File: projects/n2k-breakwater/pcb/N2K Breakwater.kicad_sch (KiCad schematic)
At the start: 44 parts, among them J1 Shield to Ground, J2 N2K, J3 Signals, J4 Power, Q1 SQJ872EP-T1_BE3, Q2 SQJ872EP-T1_BE3, Q3 BSS123NH6327XTSA1, Q4 BSS126H6327XTSA2

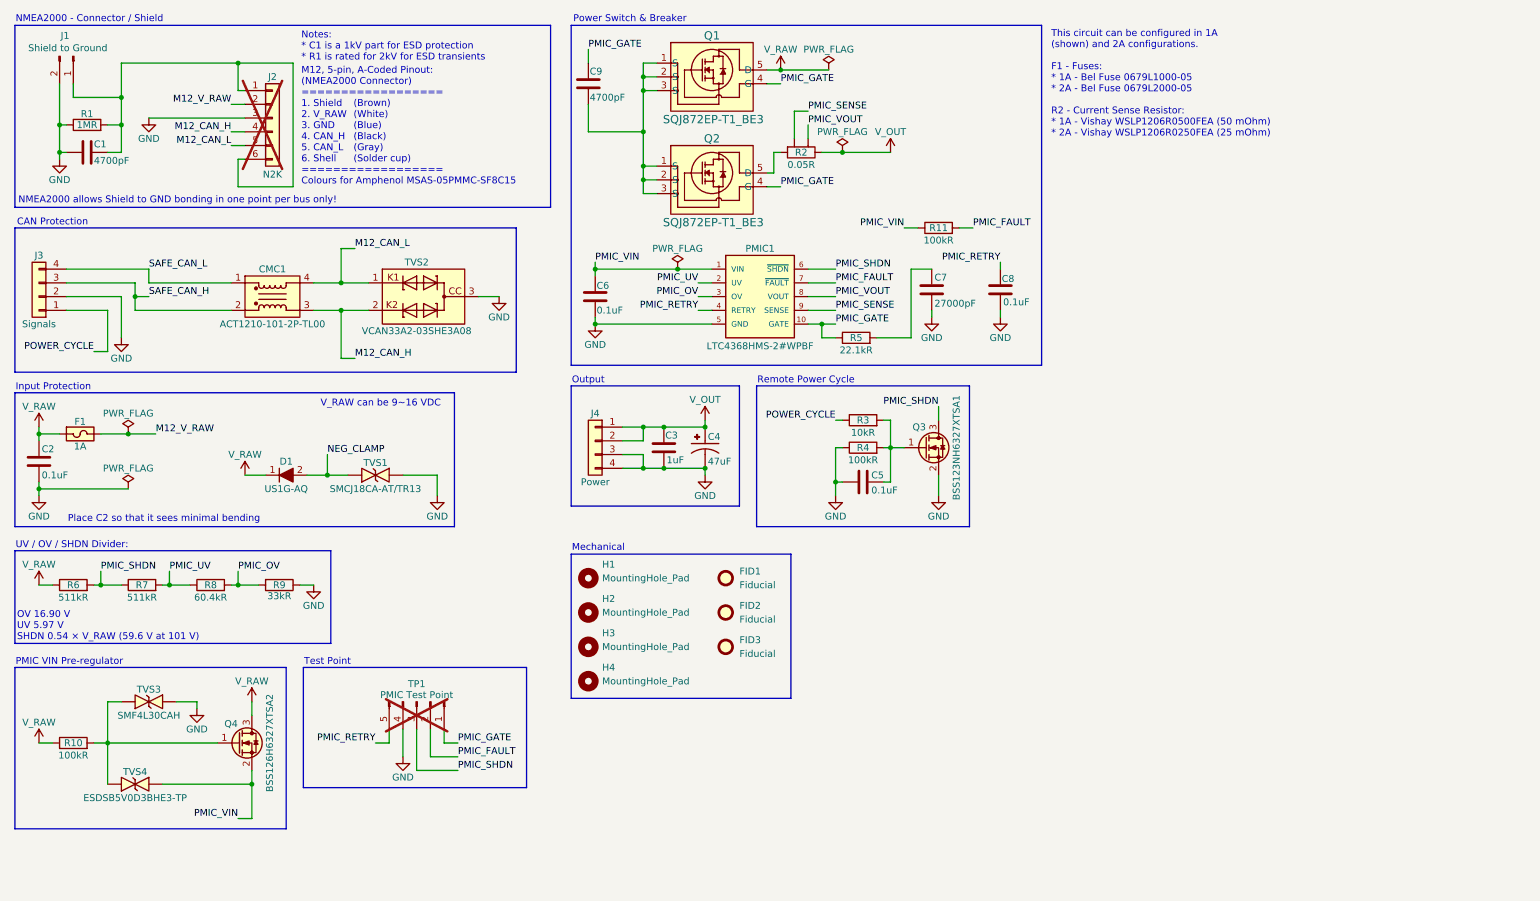
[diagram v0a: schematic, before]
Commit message: Added zip-tie slots to allow strain relief.
Signed-off-by: digimer <digital.mermaid@gmail.com>
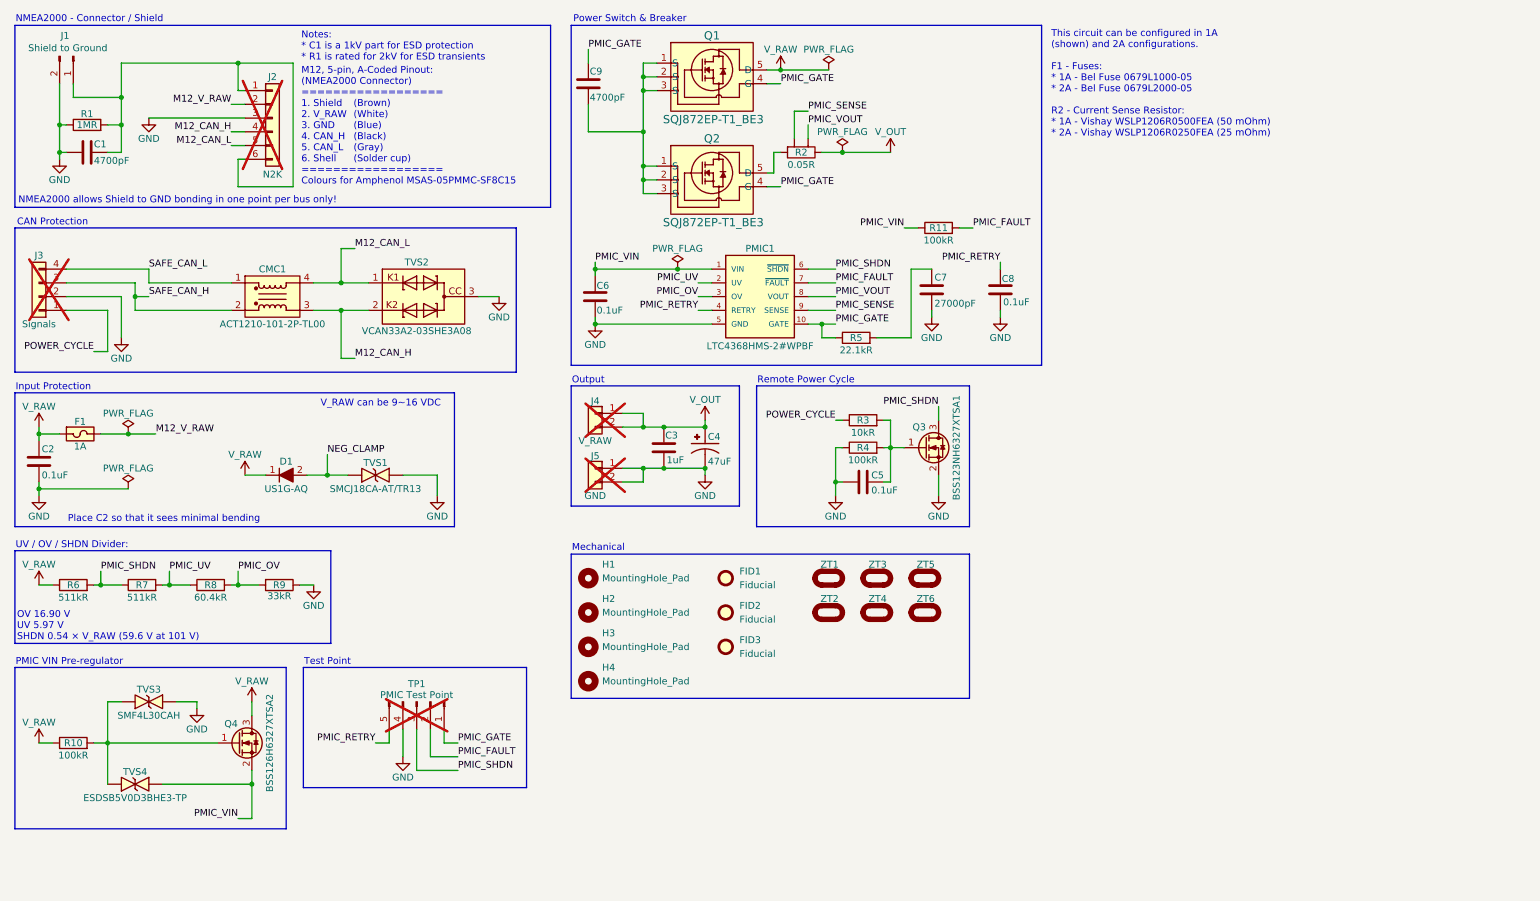
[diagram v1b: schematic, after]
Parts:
- removed J4: Power, Connector_PinHeader_2.54mm:PinHeader_1x04_P2.54mm_Vertical, symbol Connector_Generic:Conn_01x04
- added J4: V_RAW, Connector_PinHeader_2.54mm:PinHeader_1x02_P2.54mm_Vertical, symbol Connector_Generic:Conn_01x02
- added J5: GND, Connector_PinHeader_2.54mm:PinHeader_1x02_P2.54mm_Vertical, symbol Connector_Generic:Conn_01x02
- added ZT1, ZT2, ZT3, ZT4, ZT5, ZT6: (no value), mr-stuff:Tuskar Ziptie Slot 4.5x2mm, symbol mr-parts:Tuskar Ziptie slot 4.5x2mm
- J3: now not fitted; now left out of the parts list
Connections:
- net GND: now also J5.1 (Pin_1), J5.2 (Pin_2)
- net V_OUT: now also J4.1 (Pin_1), J4.2 (Pin_2)

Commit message: Fixed DRC issues.
Signed-off-by: digimer <digital.mermaid@gmail.com>
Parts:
- renumbered C9 to C3, C6 to C4, C7 to C5, C8 to C6, C3 to C7, C4 to C8, C5 to C9, Q4 to Q1, Q1 to Q2, Q2 to Q3, Q3 to Q4, R3 to R10, R4 to R11, R6 to R2, R7 to R3, R8 to R4, R9 to R5, R10 to R6, R2 to R7, R11 to R8, R5 to R9, TVS2 to TVS1, TVS1 to TVS2
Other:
- note added: "This circuit can be configured in 1A (shown) and 2A configurations. F1 - Fuses: * 1A - Bel Fuse 0679L1000-05 * 2A - Bel Fuse 0679L2000-05 R7 - Current Sense Resistor: * 1A - Vishay WSLP1206R0500FEA (50 mOhm) * 2A - Vishay WSLP1206R0250FEA (25 mOhm)"
- note removed: "This circuit can be configured in 1A (shown) and 2A configurations. F1 - Fuses: * 1A - Bel Fuse 0679L1000-05 * 2A - Bel Fuse 0679L2000-05 R2 - Current Sense Resistor: * 1A - Vishay WSLP1206R0500FEA (50 mOhm) * 2A - Vishay WSLP1206R0250FEA (25 mOhm)"
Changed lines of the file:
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@@
 		)
 	)
-	(text "This circuit can be configured in 1A \n(shown) and 2A configurations.\n\nF1 - Fuses:\n* 1A - Bel Fuse 0679L1000-05\n* 2A - Bel Fuse 0679L2000-05\n\nR2 - Current Sense Resistor:\n* 1A - Vishay WSLP1206R0500FEA (50 mOhm)\n* 2A - Vishay WSLP1206R0250FEA (25 mOhm)"
+	(text "This circuit can be configured in 1A \n(shown) and 2A configurations.\n\nF1 - Fuses:\n* 1A - Bel Fuse 0679L1000-05\n* 2A - Bel Fuse 0679L2000-05\n\nR7 - Current Sense Resistor:\n* 1A - Vishay WSLP1206R0500FEA (50 mOhm)\n* 2A - Vishay WSLP1206R0250FEA (25 mOhm)"
 		(exclude_from_sim no)
 		(at 206.248 16.764 0)
@@
 		(in_pos_files yes)
 		(dnp no)
-		(property "Reference" "R4"
+		(property "Reference" "R11"
 			(at 171.45 93.98 0)
 			(show_name no)
@@
 			(project "N2K Breakwater"
 				(path "/2a070473-cb6e-4844-8f2a-5ea6a35ddb49"
-					(reference "R4")
+					(reference "R11")
 					(unit 1)
 				)
@@
 		(in_pos_files yes)
 		(dnp no)
-		(property "Reference" "Q3"
+		(property "Reference" "Q4"
 			(at 180.594 90.17 0)
 			(show_name no)
@@
 			(project "N2K Breakwater"
 				(path "/2a070473-cb6e-4844-8f2a-5ea6a35ddb49"
-					(reference "Q3")
+					(reference "Q4")
 					(unit 1)
 				)
@@
 		(in_pos_files yes)
 		(dnp no)
-		(property "Reference" "Q2"
+		(property "Reference" "Q3"
 			(at 143.51 36.83 0)
 			(show_name no)
@@
 			(project "N2K Breakwater"
 				(path "/2a070473-cb6e-4844-8f2a-5ea6a35ddb49"
-					(reference "Q2")
+					(reference "Q3")
 					(unit 1)
 				)
@@
 		(in_pos_files yes)
 		(dnp no)
-		(property "Reference" "C5"
+		(property "Reference" "C9"
 			(at 172.974 99.06 90)
 			(show_name no)
@@
 			(project "N2K Breakwater"
 				(path "/2a070473-cb6e-4844-8f2a-5ea6a35ddb49"
-					(reference "C5")
+					(reference "C9")
 					(unit 1)
 				)
@@
 		(in_pos_files yes)
 		(dnp no)
-		(property "Reference" "R9"
+		(property "Reference" "R5"
 			(at 63.5 119.38 0)
 			(show_name no)
@@
 			(project "N2K Breakwater"
 				(path "/2a070473-cb6e-4844-8f2a-5ea6a35ddb49"
-					(reference "R9")
+					(reference "R5")
 					(unit 1)
 				)
@@
 		(in_pos_files yes)
 		(dnp no)
-		(property "Reference" "C7"
+		(property "Reference" "C5"
 			(at 184.658 62.484 0)
 			(show_name no)
@@
 			(project "N2K Breakwater"
 				(path "/2a070473-cb6e-4844-8f2a-5ea6a35ddb49"
-					(reference "C7")
+					(reference "C5")
 					(unit 1)
 				)
@@
 		(in_pos_files yes)
 		(dnp no)
-		(property "Reference" "Q1"
+		(property "Reference" "Q2"
 			(at 143.51 17.78 0)
 			(show_name no)
@@
 			(project "N2K Breakwater"
 				(path "/2a070473-cb6e-4844-8f2a-5ea6a35ddb49"
-					(reference "Q1")
+					(reference "Q2")
 					(unit 1)
 				)
@@
 		(in_pos_files yes)
 		(dnp no)
-		(property "Reference" "Q4"
+		(property "Reference" "Q1"
 			(at 53.34 145.034 0)
 			(show_name no)
@@
 			(project "N2K Breakwater"
 				(path "/2a070473-cb6e-4844-8f2a-5ea6a35ddb49"
-					(reference "Q4")
+					(reference "Q1")
 					(unit 1)
 				)
@@
 		(in_pos_files yes)
 		(dnp no)
-		(property "Reference" "C3"
+		(property "Reference" "C7"
 			(at 134.874 91.694 0)
 			(show_name no)
@@
 			(project "N2K Breakwater"
 				(path "/2a070473-cb6e-4844-8f2a-5ea6a35ddb49"
-					(reference "C3")
+					(reference "C7")
 					(unit 1)
 				)
@@
 		(in_pos_files yes)
 		(dnp no)
-		(property "Reference" "R8"
+		(property "Reference" "R4"
 			(at 50.8 119.38 0)
 			(show_name no)
@@
 			(project "N2K Breakwater"
 				(path "/2a070473-cb6e-4844-8f2a-5ea6a35ddb49"
-					(reference "R8")
+					(reference "R4")
 					(unit 1)
 				)
@@
 		(in_pos_files yes)
 		(dnp no)
-		(property "Reference" "R6"
+		(property "Reference" "R2"
 			(at 25.4 119.38 0)
 			(show_name no)
@@
 			(project "N2K Breakwater"
 				(path "/2a070473-cb6e-4844-8f2a-5ea6a35ddb49"
-					(reference "R6")
+					(reference "R2")
 					(unit 1)
 				)
@@
 		(in_pos_files yes)
 		(dnp no)
-		(property "Reference" "C6"
+		(property "Reference" "C4"
 			(at 122.174 64.008 0)
 			(show_name no)
@@
 			(project "N2K Breakwater"
 				(path "/2a070473-cb6e-4844-8f2a-5ea6a35ddb49"
-					(reference "C6")
+					(reference "C4")
 					(unit 1)
 				)
@@
 		(in_pos_files yes)
 		(dnp no)
-		(property "Reference" "C8"
+		(property "Reference" "C6"
 			(at 197.104 62.738 0)
 			(show_name no)
@@
 			(project "N2K Breakwater"
 				(path "/2a070473-cb6e-4844-8f2a-5ea6a35ddb49"
-					(reference "C8")
+					(reference "C6")
 					(unit 1)
 				)
@@
 		(in_pos_files yes)
 		(dnp no)
-		(property "Reference" "R2"
+		(property "Reference" "R7"
 			(at 160.02 39.37 0)
 			(show_name no)
@@
 			(project "N2K Breakwater"
 				(path "/2a070473-cb6e-4844-8f2a-5ea6a35ddb49"
-					(reference "R2")
+					(reference "R7")
 					(unit 1)
 				)
@@
 		(in_pos_files yes)
 		(dnp no)
-		(property "Reference" "R5"
+		(property "Reference" "R9"
 			(at 170.18 73.66 0)
 			(show_name no)
@@
 			(project "N2K Breakwater"
 				(path "/2a070473-cb6e-4844-8f2a-5ea6a35ddb49"
-					(reference "R5")
+					(reference "R9")
 					(unit 1)
 				)
@@
 		(in_pos_files yes)
 		(dnp no)
-		(property "Reference" "R11"
+		(property "Reference" "R8"
 			(at 185.42 53.34 0)
 			(show_name no)
@@
 			(project "N2K Breakwater"
 				(path "/2a070473-cb6e-4844-8f2a-5ea6a35ddb49"
-					(reference "R11")
+					(reference "R8")
 					(unit 1)
 				)
@@
 		(in_pos_files yes)
 		(dnp no)
-		(property "Reference" "TVS1"
+		(property "Reference" "TVS2"
 			(at 81.28 96.774 0)
 			(show_name no)
@@
 			(project "N2K Breakwater"
 				(path "/2a070473-cb6e-4844-8f2a-5ea6a35ddb49"
-					(reference "TVS1")
+					(reference "TVS2")
 					(unit 1)
 				)
@@
 		(in_pos_files yes)
 		(dnp no)
-		(property "Reference" "C9"
+		(property "Reference" "C3"
 			(at 120.904 24.384 0)
 			(show_name no)
@@
 			(project "N2K Breakwater"
 				(path "/2a070473-cb6e-4844-8f2a-5ea6a35ddb49"
-					(reference "C9")
+					(reference "C3")
 					(unit 1)
 				)
@@
 		(in_pos_files yes)
 		(dnp no)
-		(property "Reference" "TVS2"
+		(property "Reference" "TVS1"
 			(at 88.9 59.69 0)
 			(show_name no)
@@
 			(project "N2K Breakwater"
 				(path "/2a070473-cb6e-4844-8f2a-5ea6a35ddb49"
-					(reference "TVS2")
+					(reference "TVS1")
 					(unit 1)
 				)
@@
 		(in_pos_files yes)
 		(dnp no)
-		(property "Reference" "R7"
+		(property "Reference" "R3"
 			(at 38.1 119.38 0)
 			(show_name no)
@@
 			(project "N2K Breakwater"
 				(path "/2a070473-cb6e-4844-8f2a-5ea6a35ddb49"
-					(reference "R7")
+					(reference "R3")
 					(unit 1)
 				)
@@
 		(in_pos_files yes)
 		(dnp no)
-		(property "Reference" "R10"
+		(property "Reference" "R6"
 			(at 25.4 148.59 0)
 			(show_name no)
@@
 			(project "N2K Breakwater"
 				(path "/2a070473-cb6e-4844-8f2a-5ea6a35ddb49"
-					(reference "R10")
+					(reference "R6")
 					(unit 1)
 				)
@@
 		(in_pos_files yes)
 		(dnp no)
-		(property "Reference" "R3"
+		(property "Reference" "R10"
 			(at 171.45 88.9 0)
 			(show_name no)
@@
 			(project "N2K Breakwater"
 				(path "/2a070473-cb6e-4844-8f2a-5ea6a35ddb49"
-					(reference "R3")
+					(reference "R10")
 					(unit 1)
 				)
@@
 		(in_pos_files yes)
 		(dnp no)
-		(property "Reference" "C4"
+		(property "Reference" "C8"
 			(at 142.748 91.948 90)
 			(show_name no)
@@
 			(project "N2K Breakwater"
 				(path "/2a070473-cb6e-4844-8f2a-5ea6a35ddb49"
-					(reference "C4")
+					(reference "C8")
 					(unit 1)
 				)

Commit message: Fixed J4's label to 'V_OUT'.
Signed-off-by: digimer <digital.mermaid@gmail.com>
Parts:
- J4: value V_RAW -> V_OUT
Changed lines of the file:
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@@
 			)
 		)
-		(property "Value" "V_RAW"
+		(property "Value" "V_OUT"
 			(at 121.92 92.71 0)
 			(show_name no)

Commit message: Reworked the PCB and F1+R7 values.
Signed-off-by: digimer <digital.mermaid@gmail.com>
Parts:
- removed J2: N2K, Connector_PinHeader_2.54mm:PinHeader_1x06_P2.54mm_Vertical, symbol Connector_Generic:Conn_01x06
- removed ZT5, ZT6: (no value), mr-stuff:Tuskar Ziptie Slot 4.5x2mm, symbol mr-parts:Tuskar Ziptie slot 4.5x2mm
- added J2: Shell, Connector_PinHeader_2.54mm:PinHeader_1x01_P2.54mm_Vertical, symbol Connector_Generic:Conn_01x01
- added TB1: 1862440, mr-stuff:Phoenix Contact 1862440, symbol mr-parts:Phoenix Contact 1862440
- F1: value 1A -> 2.5A; symbol mr-parts:Bel Fuse 0679L1000-05 -> mr-parts:Bel Fuse 0679L2500-05; Part Bel Fuse 0679L1000-05 -> Bel Fuse 0679L2500-05
- R7: value 0.05R -> 0.033R; footprint mr-stuff:Vishay WSLP 1206 4-wire Kelvin -> mr-stuff:Vishay RCWE 1206 4-wire Kelvin; symbol mr-parts:Vishay WSLP1206R0500FEA -> mr-parts:Vishay RCWE120633L0FNEA; Part Vishay WSLP1206R0500FEA -> Vishay RCWE120633L0FNEA
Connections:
- net GND: now also J3.3 (Pin_3), TB1.5, TB1.6; no longer J3.2 (Pin_2)
- net M12_CAN_H: now also TB1.7, TB1.8
- net M12_CAN_L: now also TB1.10, TB1.9
- net M12_V_RAW: now also TB1.3, TB1.4
- net POWER_CYCLE: now also J3.4 (Pin_4); no longer J3.1 (Pin_1)
- net SAFE_CAN_H: now also J3.1 (Pin_1); no longer J3.3 (Pin_3)
- net SAFE_CAN_L: now also J3.2 (Pin_2); no longer J3.4 (Pin_4)
- net at C1.2, J1.1 (Pin_1), R1.2: now also J2.1 (Pin_1), TB1.1, TB1.2
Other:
- note added: "- Brown - White - Blue - Black - Gray"
- note added: "M12, 5-pin, A-Coded Pinout: (NMEA2000 Connector) ================== 1. Shield 2. V_RAW 3. GND 4. CAN_H 5. CAN_L ================== Colours for Amphenol MSAS-05PMMC-SF8C15 * Tie M12 shell to ship's ground for ESD"
- note added: "Notes: * C1 is a 1kV part for ESD protection * R1 is rated for 2kV for ESD transients * J1 connects to MSAS-05PMMC-SF8C15 Shell Solder Cup"
- note added: "This circuit shows the 2.5A configurations. Trip Point Configs; 1A: * F1 - Bel Fuse 0679L1000-05 (1A Fast Blow) * R7 - Vishay RCWE1206R100FKEA (100 mΩ, min 0.40A / typ 0.50A / max 0.60A) 2.5A: * F1 - Bel Fuse 0679L2500-05 (2.5A Fast Blow) * R7 - Vishay RCWE120633L0FNEA (33 mΩ, min 1.21A / typ 1.52A / max 1.82A)"
- note removed: "(Brown) (White) (Blue) (Black) (Gray) (Solder cup)"
- note removed: "M12, 5-pin, A-Coded Pinout: (NMEA2000 Connector) ================== 1. Shield 2. V_RAW 3. GND 4. CAN_H 5. CAN_L 6. Shell ================== Colours for Amphenol MSAS-05PMMC-SF8C15"
- note removed: "Notes: * C1 is a 1kV part for ESD protection * R1 is rated for 2kV for ESD transients"
- note removed: "This circuit can be configured in 1A (shown) and 2A configurations. F1 - Fuses: * 1A - Bel Fuse 0679L1000-05 * 2A - Bel Fuse 0679L2000-05 R7 - Current Sense Resistor: * 1A - Vishay WSLP1206R0500FEA (50 mOhm) * 2A - Vishay WSLP1206R0250FEA (25 mOhm)"
- moved on the sheet: C1, C2, C3, C4, C5, C6, C7, C8, C9, CMC1, D1, F1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
